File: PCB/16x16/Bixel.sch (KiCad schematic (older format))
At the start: 261 parts, among them J1 Conn_01x22, J2 Screw_Terminal_01x02, U1 74HC595, U2 74HC595

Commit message: More work on PCB layout
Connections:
- net CI: now also J1.6 (Pin_6); no longer J1.21 (Pin_21)
- net CLOCK: now also J1.2 (Pin_2); no longer J1.18 (Pin_18)
- net DATA: now also J1.1 (Pin_1); no longer J1.17 (Pin_17)
- net DI: now also J1.5 (Pin_5); no longer J1.20 (Pin_20)
- net GND: now also J1.4 (Pin_4); no longer J1.22 (Pin_22)
- net LATCH: now also J1.3 (Pin_3); no longer J1.19 (Pin_19)
- net ROW_0: now also J1.7 (Pin_7); no longer J1.1 (Pin_1)
- net ROW_1: now also J1.8 (Pin_8); no longer J1.2 (Pin_2)
- net ROW_10: now also J1.17 (Pin_17); no longer J1.11 (Pin_11)
- net ROW_11: now also J1.18 (Pin_18); no longer J1.12 (Pin_12)
- net ROW_12: now also J1.19 (Pin_19); no longer J1.13 (Pin_13)
- net ROW_13: now also J1.20 (Pin_20); no longer J1.14 (Pin_14)
- net ROW_14: now also J1.21 (Pin_21); no longer J1.15 (Pin_15)
- net ROW_15: now also J1.22 (Pin_22); no longer J1.16 (Pin_16)
- net ROW_2: now also J1.9 (Pin_9); no longer J1.3 (Pin_3)
- net ROW_3: now also J1.10 (Pin_10); no longer J1.4 (Pin_4)
- net ROW_4: now also J1.11 (Pin_11); no longer J1.5 (Pin_5)
- net ROW_5: now also J1.12 (Pin_12); no longer J1.6 (Pin_6)
- net ROW_6: now also J1.13 (Pin_13); no longer J1.7 (Pin_7)
- net ROW_7: now also J1.14 (Pin_14); no longer J1.8 (Pin_8)
- net ROW_8: now also J1.15 (Pin_15); no longer J1.9 (Pin_9)
- net ROW_9: now also J1.16 (Pin_16); no longer J1.10 (Pin_10)
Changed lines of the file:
@@
 Wire Wire Line
 	26050 4150 26150 4150
+Text GLabel 24400 6000 0    51   Input ~ 0
+ROW_0
+Text GLabel 24400 6100 0    51   Input ~ 0
+ROW_1
+Text GLabel 24400 6200 0    51   Input ~ 0
+ROW_2
+Text GLabel 24400 6300 0    51   Input ~ 0
+ROW_3
+Text GLabel 24400 6400 0    51   Input ~ 0
+ROW_4
+Text GLabel 24400 6500 0    51   Input ~ 0
+ROW_5
+Text GLabel 24400 6600 0    51   Input ~ 0
+ROW_6
+Text GLabel 24400 6700 0    51   Input ~ 0
+ROW_7
+Text GLabel 24400 6800 0    51   Input ~ 0
+ROW_8
+Text GLabel 24400 6900 0    51   Input ~ 0
+ROW_9
+Text GLabel 24400 7000 0    51   Input ~ 0
+ROW_10
+Text GLabel 24400 7100 0    51   Input ~ 0
+ROW_11
+Text GLabel 24400 7200 0    51   Input ~ 0
+ROW_12
+Text GLabel 24400 7300 0    51   Input ~ 0
+ROW_13
+Text GLabel 24400 7400 0    51   Input ~ 0
+ROW_14
+Text GLabel 24400 7500 0    51   Input ~ 0
+ROW_15
 Text GLabel 24400 5400 0    51   Input ~ 0
-ROW_0
+DATA
 Text GLabel 24400 5500 0    51   Input ~ 0
-ROW_1
+CLOCK
 Text GLabel 24400 5600 0    51   Input ~ 0
-ROW_2
+LATCH
 Text GLabel 24400 5700 0    51   Input ~ 0
-ROW_3
-Text GLabel 24400 5800 0    51   Input ~ 0
-ROW_4
-Text GLabel 24400 5900 0    51   Input ~ 0
-ROW_5
-Text GLabel 24400 6000 0    51   Input ~ 0
-ROW_6
-Text GLabel 24400 6100 0    51   Input ~ 0
-ROW_7
-Text GLabel 24400 6200 0    51   Input ~ 0
-ROW_8
-Text GLabel 24400 6300 0    51   Input ~ 0
-ROW_9
-Text GLabel 24400 6400 0    51   Input ~ 0
-ROW_10
-Text GLabel 24400 6500 0    51   Input ~ 0
-ROW_11
-Text GLabel 24400 6600 0    51   Input ~ 0
-ROW_12
-Text GLabel 24400 6700 0    51   Input ~ 0
-ROW_13
-Text GLabel 24400 6800 0    51   Input ~ 0
-ROW_14
-Text GLabel 24400 6900 0    51   Input ~ 0
-ROW_15
-Text GLabel 24400 7000 0    51   Input ~ 0
-DATA
-Text GLabel 24400 7100 0    51   Input ~ 0
-CLOCK
-Text GLabel 24400 7200 0    51   Input ~ 0
-LATCH
-Text GLabel 24400 7500 0    51   Input ~ 0
 GND
 $Comp
@@
 	1    0    0    -1
 $EndComp
-Text GLabel 24400 7300 0    51   Input ~ 0
+Text GLabel 24400 5800 0    51   Input ~ 0
 DI
-Text GLabel 24400 7400 0    51   Input ~ 0
+Text GLabel 24400 5900 0    51   Input ~ 0
 CI
 Text GLabel 8000 2350 1    51   Input ~ 0

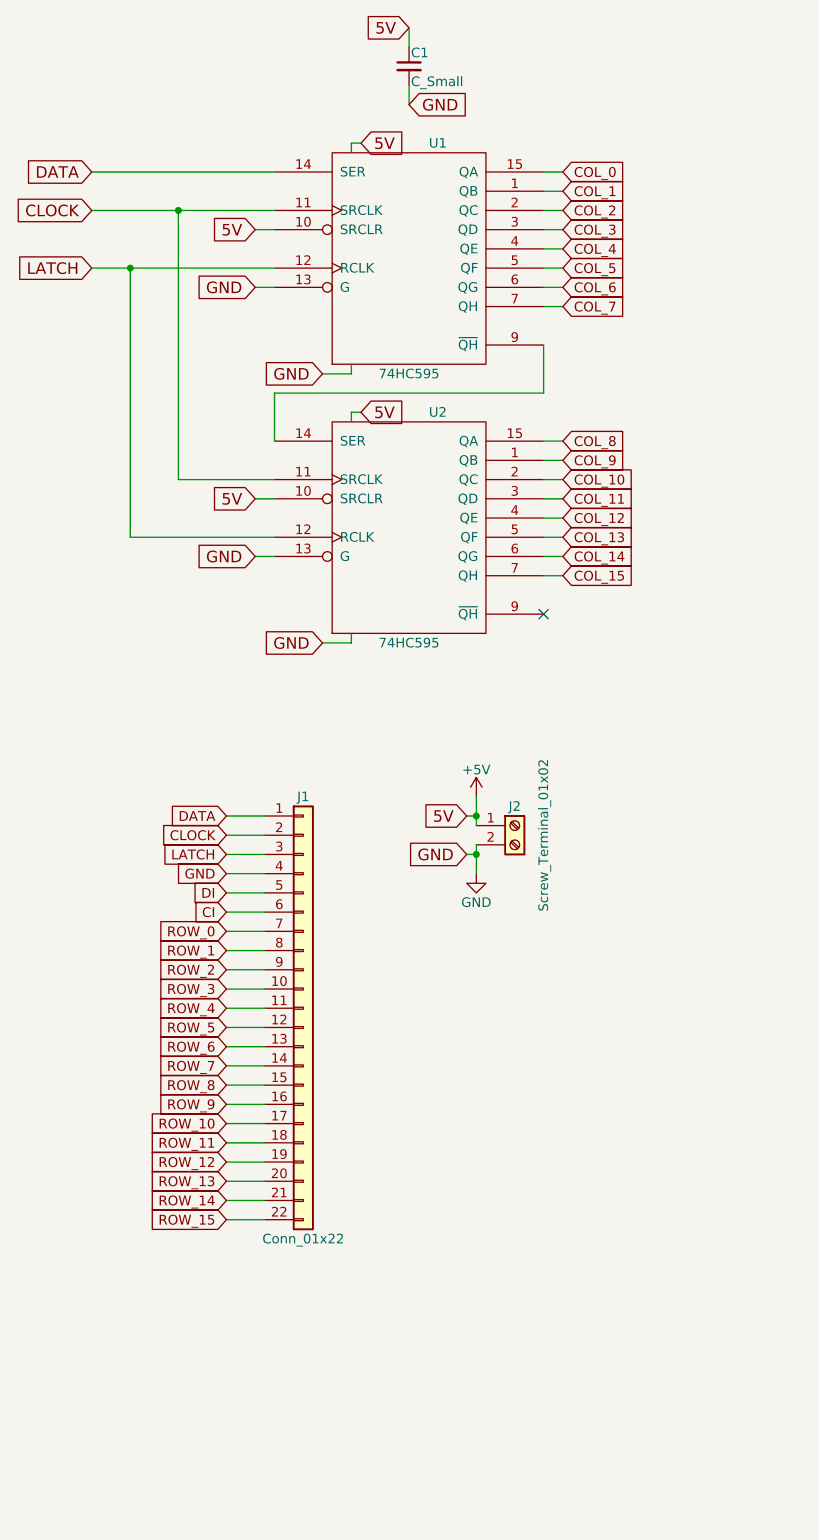
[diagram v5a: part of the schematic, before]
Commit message: Yet more work on Bixel layout. Added 2x12 header, 3V3 for shifters
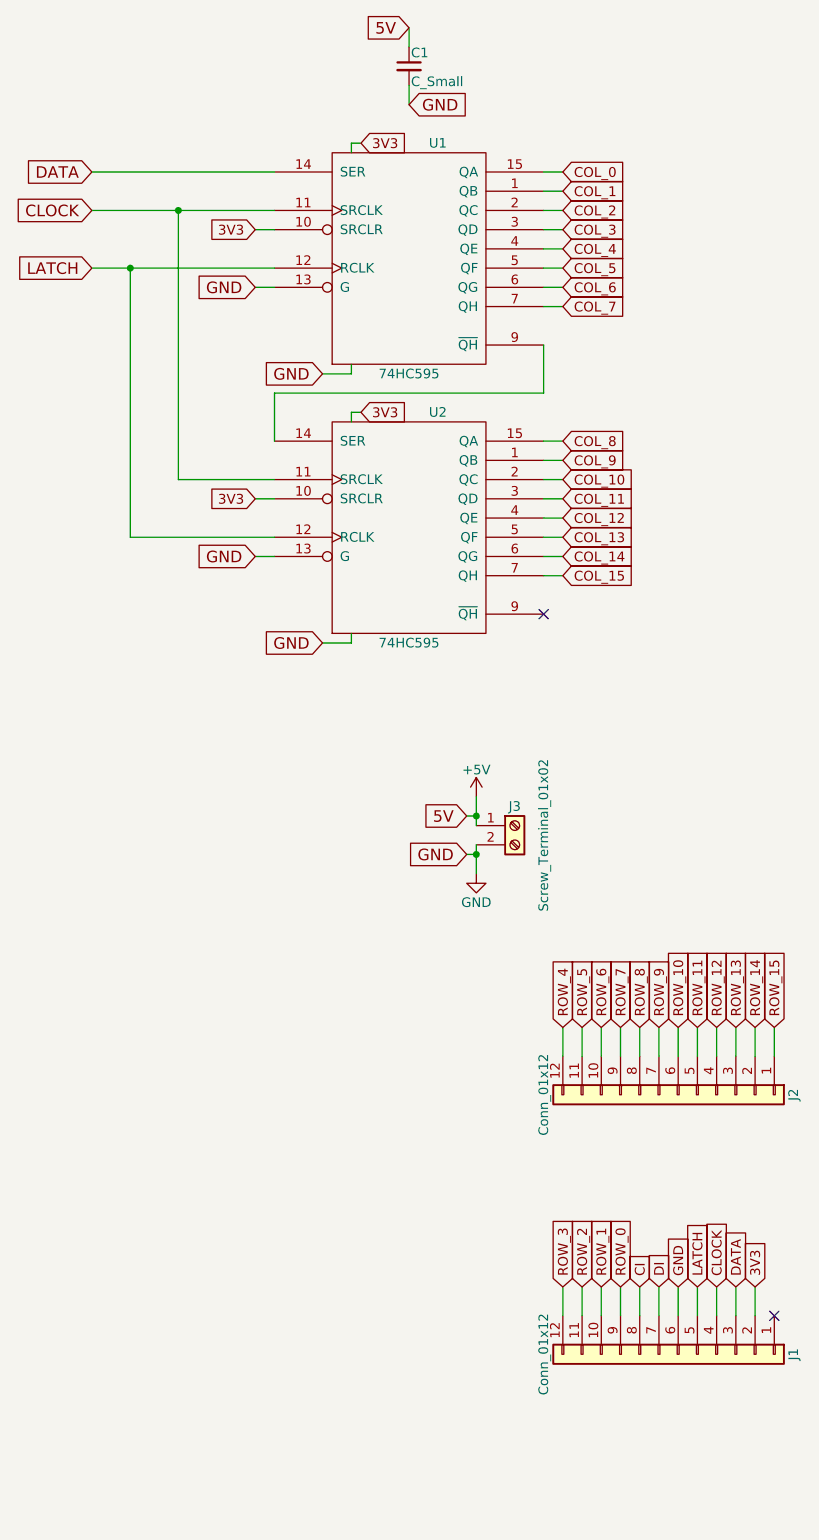
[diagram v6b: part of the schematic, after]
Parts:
- removed J1: Conn_01x22, Pin_Headers:Pin_Header_Straight_1x22_Pitch2.54mm, symbol Conn_01x22
- added J1, J2: Conn_01x12, Pin_Headers:Pin_Header_Straight_1x12_Pitch2.54mm, symbol Conn_01x12
- renumbered J2 to J3
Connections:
- net +5V: no longer U1.10 (SRCLR), U1.16 (VCC), U2.10 (SRCLR), U2.16 (VCC)
- net CI: now also J1.8 (Pin_8)
- net CLOCK: now also J1.4 (Pin_4)
- net DATA: now also J1.3 (Pin_3)
- net DI: now also J1.7 (Pin_7)
- net GND: now also J1.6 (Pin_6)
- net LATCH: now also J1.5 (Pin_5)
- net ROW_0: now also J1.9 (Pin_9)
- net ROW_1: now also J1.10 (Pin_10)
- net ROW_10: now also J2.6 (Pin_6)
- net ROW_11: now also J2.5 (Pin_5)
- net ROW_12: now also J2.4 (Pin_4)
- net ROW_13: now also J2.3 (Pin_3)
- net ROW_14: now also J2.2 (Pin_2)
- net ROW_15: now also J2.1 (Pin_1)
- net ROW_2: now also J1.11 (Pin_11)
- net ROW_3: now also J1.12 (Pin_12)
- net ROW_4: now also J2.12 (Pin_12)
- net ROW_5: now also J2.11 (Pin_11)
- net ROW_6: now also J2.10 (Pin_10)
- net ROW_7: now also J2.9 (Pin_9)
- net ROW_8: now also J2.8 (Pin_8)
- net ROW_9: now also J2.7 (Pin_7)
- new net VCC: J1.2 (Pin_2), U1.10 (SRCLR), U1.16 (VCC), U2.10 (SRCLR), U2.16 (VCC)
- no-connect marks 5 -> 6
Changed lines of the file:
@@
 Text GLabel 23700 2550 0    60   Input ~ 0
 LATCH
-Text GLabel 25100 1900 2    60   Input ~ 0
-5V
 Wire Wire Line
 	7800 3450 7800 3600
@@
 Wire Wire Line
 	26050 4150 26150 4150
-Text GLabel 24400 6000 0    51   Input ~ 0
+Text GLabel 26450 7850 1    51   Input ~ 0
 ROW_0
-Text GLabel 24400 6100 0    51   Input ~ 0
+Text GLabel 26350 7850 1    51   Input ~ 0
 ROW_1
-Text GLabel 24400 6200 0    51   Input ~ 0
+Text GLabel 26250 7850 1    51   Input ~ 0
 ROW_2
-Text GLabel 24400 6300 0    51   Input ~ 0
+Text GLabel 26150 7850 1    51   Input ~ 0
 ROW_3
-Text GLabel 24400 6400 0    51   Input ~ 0
+Text GLabel 26150 6500 1    51   Input ~ 0
 ROW_4
-Text GLabel 24400 6500 0    51   Input ~ 0
+Text GLabel 26250 6500 1    51   Input ~ 0
 ROW_5
-Text GLabel 24400 6600 0    51   Input ~ 0
+Text GLabel 26350 6500 1    51   Input ~ 0
 ROW_6
-Text GLabel 24400 6700 0    51   Input ~ 0
+Text GLabel 26450 6500 1    51   Input ~ 0
 ROW_7
-Text GLabel 24400 6800 0    51   Input ~ 0
+Text GLabel 26550 6500 1    51   Input ~ 0
 ROW_8
-Text GLabel 24400 6900 0    51   Input ~ 0
+Text GLabel 26650 6500 1    51   Input ~ 0
 ROW_9
-Text GLabel 24400 7000 0    51   Input ~ 0
+Text GLabel 26750 6500 1    51   Input ~ 0
 ROW_10
-Text GLabel 24400 7100 0    51   Input ~ 0
+Text GLabel 26850 6500 1    51   Input ~ 0
 ROW_11
-Text GLabel 24400 7200 0    51   Input ~ 0
+Text GLabel 26950 6500 1    51   Input ~ 0
 ROW_12
-Text GLabel 24400 7300 0    51   Input ~ 0
+Text GLabel 27050 6500 1    51   Input ~ 0
 ROW_13
-Text GLabel 24400 7400 0    51   Input ~ 0
+Text GLabel 27150 6500 1    51   Input ~ 0
 ROW_14
-Text GLabel 24400 7500 0    51   Input ~ 0
+Text GLabel 27250 6500 1    51   Input ~ 0
 ROW_15
-Text GLabel 24400 5400 0    51   Input ~ 0
+Text GLabel 27050 7850 1    51   Input ~ 0
 DATA
-Text GLabel 24400 5500 0    51   Input ~ 0
+Text GLabel 26950 7850 1    51   Input ~ 0
 CLOCK
-Text GLabel 24400 5600 0    51   Input ~ 0
+Text GLabel 26850 7850 1    51   Input ~ 0
 LATCH
-Text GLabel 24400 5700 0    51   Input ~ 0
+Text GLabel 26750 7850 1    51   Input ~ 0
 GND
 $Comp
@@
 Wire Wire Line
 	25350 1700 25350 1600
-Text GLabel 24550 2350 0    60   Input ~ 0
-5V
 Wire Wire Line
 	24550 2350 24650 2350
@@
 Wire Wire Line
 	24550 4050 24650 4050
-Text GLabel 24550 3750 0    60   Input ~ 0
-5V
 Wire Wire Line
 	24550 3750 24650 3750
-Text GLabel 25100 3300 2    60   Input ~ 0
-5V
 Wire Wire Line
 	25050 3350 25050 3300
@@
 NoConn ~ 22350 2450
 $Comp
-L Screw_Terminal_01x02 J2
+L Screw_Terminal_01x02 J3
 U 1 1 5B4B67A7
 P 25900 5450
-F 0 "J2" H 25900 5550 50  0000 C CNN
+F 0 "J3" H 25900 5550 50  0000 C CNN
 F 1 "Screw_Terminal_01x02" V 26050 5400 50  0000 C CNN
 F 2 "TerminalBlocks_Phoenix:TerminalBlock_Phoenix_MPT-2.54mm_2pol" H 25900 5450 50  0001 C CNN
@@
 Wire Wire Line
 	25700 5600 25650 5600
-$Comp
-L Conn_01x22 J1
-U 1 1 5B4BBAF2
-P 24800 6400
-F 0 "J1" H 24800 7500 50  0000 C CNN
-F 1 "Conn_01x22" H 24800 5200 50  0000 C CNN
-F 2 "Pin_Headers:Pin_Header_Straight_1x22_Pitch2.54mm" H 24800 6400 50  0001 C CNN
-F 3 "" H 24800 6400 50  0001 C CNN
-	1    24800 6400
-	1    0    0    -1
-$EndComp
-Text GLabel 24400 5800 0    51   Input ~ 0
+Text GLabel 26650 7850 1    51   Input ~ 0
 DI
-Text GLabel 24400 5900 0    51   Input ~ 0
+Text GLabel 26550 7850 1    51   Input ~ 0
 CI
 Text GLabel 8000 2350 1    51   Input ~ 0
@@
 Wire Wire Line
 	7800 2350 7800 2450
-Wire Wire Line
-	24400 5400 24600 5400
-Wire Wire Line
-	24600 5500 24400 5500
-Wire Wire Line
-	24400 5600 24600 5600
-Wire Wire Line
-	24600 5700 24400 5700
-Wire Wire Line
-	24400 5800 24600 5800
-Wire Wire Line
-	24600 5900 24400 5900
-Wire Wire Line
-	24400 6000 24600 6000
-Wire Wire Line
-	24600 6100 24400 6100
-Wire Wire Line
-	24400 6200 24600 6200
-Wire Wire Line
-	24400 6300 24600 6300
-Wire Wire Line
-	24400 6400 24600 6400
-Wire Wire Line
-	24600 6500 24400 6500
-Wire Wire Line
-	24400 6600 24600 6600
-Wire Wire Line
-	24600 6700 24400 6700
-Wire Wire Line
-	24400 6800 24600 6800
-Wire Wire Line
-	24400 6900 24600 6900
-Wire Wire Line
-	24600 7000 24400 7000
-Wire Wire Line
-	24400 7100 24600 7100
-Wire Wire Line
-	24600 7200 24400 7200
-Wire Wire Line
-	24400 7300 24600 7300
-Wire Wire Line
-	24600 7400 24400 7400
-Wire Wire Line
-	24400 7500 24600 7500
 $Comp
 L +5V #PWR01
@@
 Wire Wire Line
 	8100 2350 8100 2450
+$Comp
+L Conn_01x12 J2
+U 1 1 5B4B52EC
+P 26750 6850
+F 0 "J2" H 26750 7450 50  0000 C CNN
+F 1 "Conn_01x12" H 26750 6150 50  0000 C CNN
+F 2 "Pin_Headers:Pin_Header_Straight_1x12_Pitch2.54mm" H 26750 6850 50  0001 C CNN
+F 3 "" H 26750 6850 50  0001 C CNN
+	1    26750 6850
+	0    1    1    0
+$EndComp
+$Comp
+L Conn_01x12 J1
+U 1 1 5B4B5947
+P 26750 8200
+F 0 "J1" H 26750 8800 50  0000 C CNN
+F 1 "Conn_01x12" H 26750 7500 50  0000 C CNN
+F 2 "Pin_Headers:Pin_Header_Straight_1x12_Pitch2.54mm" H 26750 8200 50  0001 C CNN
+F 3 "" H 26750 8200 50  0001 C CNN
+	1    26750 8200
+	0    1    1    0
+$EndComp
+Text GLabel 27150 7850 1    51   Input ~ 0
+3V3
+Text GLabel 24550 3750 0    51   Input ~ 0
+3V3
+Text GLabel 25100 3300 2    51   Input ~ 0
+3V3
+Text GLabel 24550 2350 0    51   Input ~ 0
+3V3
+Text GLabel 25100 1900 2    51   Input ~ 0
+3V3
+Wire Wire Line
+	27250 6500 27250 6650
+Wire Wire Line
+	27150 6650 27150 6500
+Wire Wire Line
+	27050 6500 27050 6650
+Wire Wire Line
+	26950 6650 26950 6500
+Wire Wire Line
+	26850 6500 26850 6650
+Wire Wire Line
+	26750 6650 26750 6500
+Wire Wire Line
+	26650 6500 26650 6650
+Wire Wire Line
+	26550 6650 26550 6500
+Wire Wire Line
+	26450 6500 26450 6650
+Wire Wire Line
+	26350 6650 26350 6500
+Wire Wire Line
+	26250 6500 26250 6650
+Wire Wire Line
+	26150 6650 26150 6500
+Wire Wire Line
+	27150 8000 27150 7850
+Wire Wire Line
+	27050 7850 27050 8000
+Wire Wire Line
+	26950 8000 26950 7850
+Wire Wire Line
+	26850 7850 26850 8000
+Wire Wire Line
+	26750 8000 26750 7850
+Wire Wire Line
+	26650 7850 26650 8000
+Wire Wire Line
+	26550 8000 26550 7850
+Wire Wire Line
+	26450 7850 26450 8000
+Wire Wire Line
+	26350 8000 26350 7850
+Wire Wire Line
+	26250 7850 26250 8000
+Wire Wire Line
+	26150 8000 26150 7850
+NoConn ~ 27250 8000
 $EndSCHEMATC

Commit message: More Layout Work
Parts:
- added C2: C_Small, Capacitors_THT:C_Disc_D5.0mm_W2.5mm_P2.50mm, symbol C_Small
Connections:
- net +5V: no longer C1.1
- net GND: now also C2.2
- net VCC: now also C1.1, C2.1
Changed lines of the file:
@@
 Text GLabel 25350 1700 2    60   Input ~ 0
 GND
-Text GLabel 25350 1300 0    60   Input ~ 0
-5V
 Wire Wire Line
 	25350 1300 25350 1400
@@
 	26150 8000 26150 7850
 NoConn ~ 27250 8000
+Text GLabel 25350 1300 0    51   Input ~ 0
+3V3
+$Comp
+L C_Small C2
+U 1 1 5B4CD9BF
+P 25400 4800
+F 0 "C2" H 25410 4870 50  0000 L CNN
+F 1 "C_Small" H 25410 4720 50  0000 L CNN
+F 2 "Capacitors_THT:C_Disc_D5.0mm_W2.5mm_P2.50mm" H 25400 4800 50  0001 C CNN
+F 3 "" H 25400 4800 50  0001 C CNN
+	1    25400 4800
+	1    0    0    -1
+$EndComp
+Text GLabel 25400 5000 2    60   Input ~ 0
+GND
+Wire Wire Line
+	25400 4600 25400 4700
+Wire Wire Line
+	25400 5000 25400 4900
+Text GLabel 25400 4600 0    51   Input ~ 0
+3V3
 $EndSCHEMATC
